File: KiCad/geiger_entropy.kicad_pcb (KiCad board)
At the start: 2 copper layers, 114.5 x 130.5 mm, 37 parts, among them J1 AudioJack2, J2 Conn_01x04_Socket, J3 Conn_01x10_Pin, J4 Conn_01x10_Pin, J5 Jack-DC, J6 ICSP, SW1 REV, SW2 FWD, SW3 RESET, U1 LM393, U2 ATmega328-P, U3 L7805, Y1 16MHz

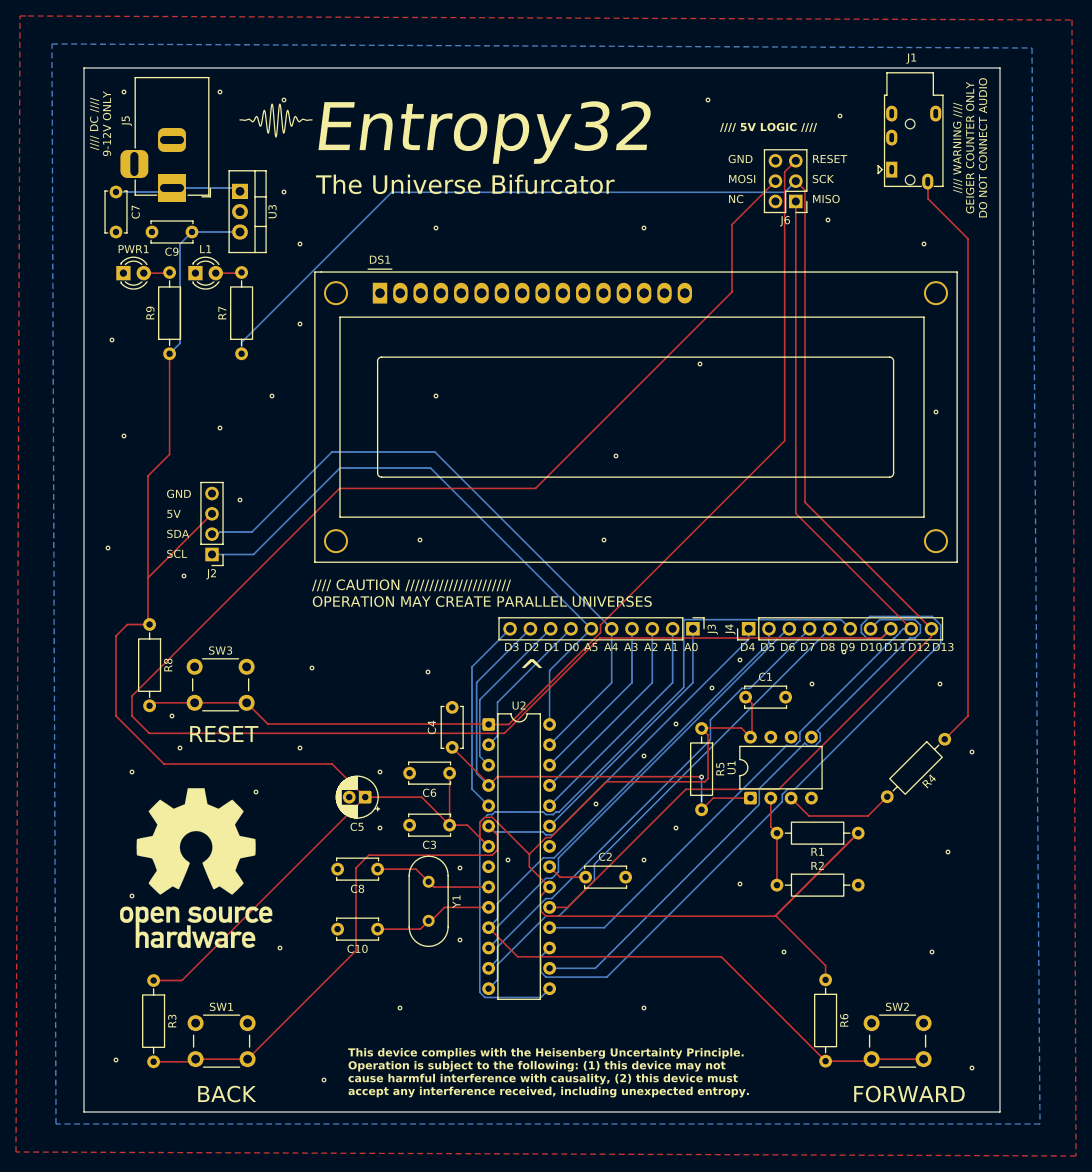
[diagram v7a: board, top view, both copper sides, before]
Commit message: Update PCB to add hysterisis to the LM393 comparator
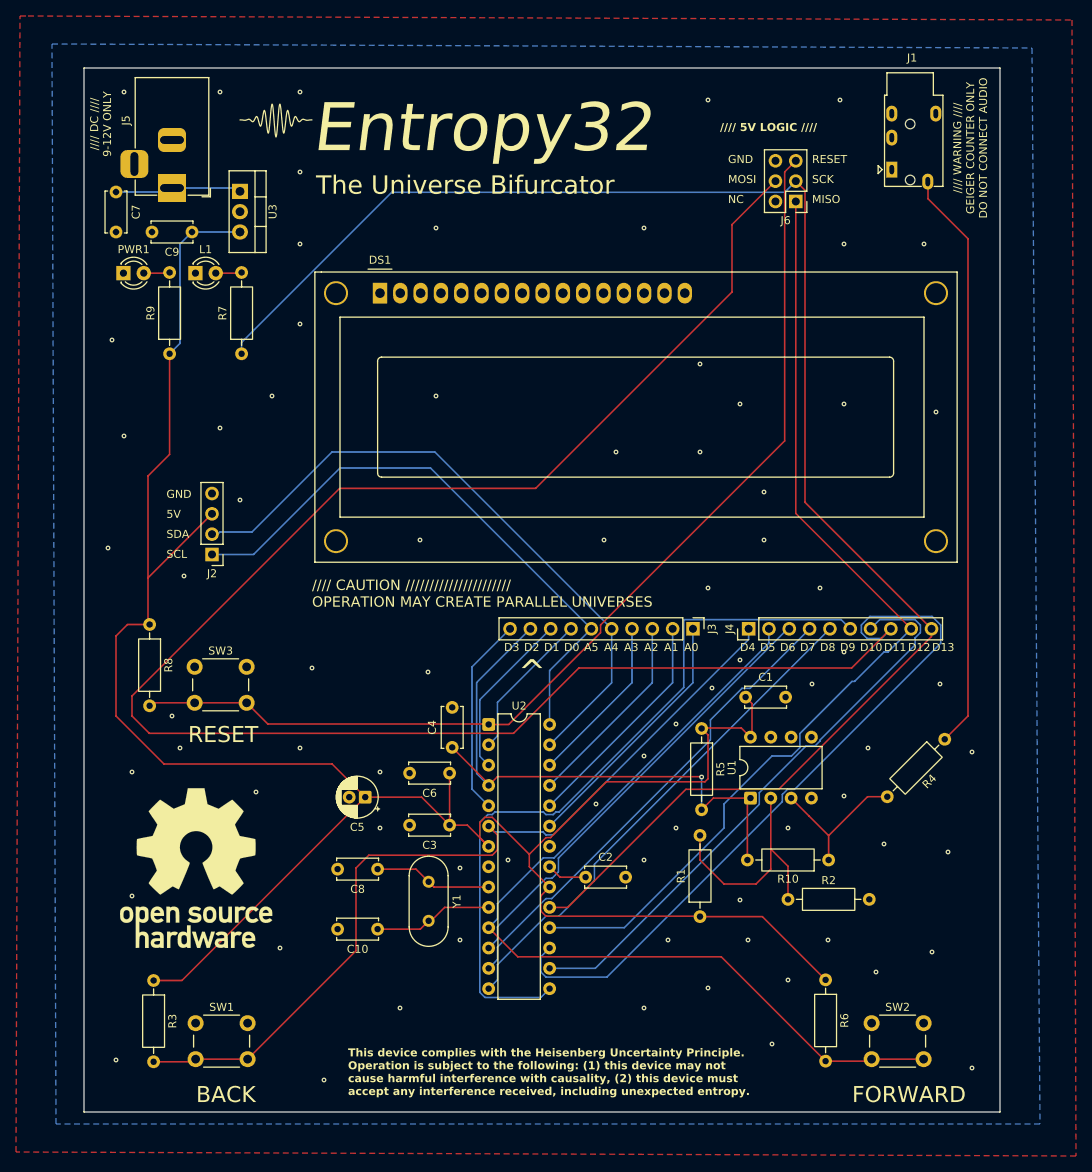
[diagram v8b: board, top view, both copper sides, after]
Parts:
- added R10: 100k, Resistor_THT:R_Axial_DIN0207_L6.3mm_D2.5mm_P10.16mm_Horizontal, F.Cu at (126.1, 127.0)
- moved R1 22.4 mm to (110.0, 134.1), turned to 90 degrees
- moved R2 2.25 mm to (121.0, 131.9)
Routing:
- net +5V: track 314.0 -> 283.8 mm
- net Net-(U1A--): track 11.2 -> 30.0 mm
- net /D2: track 67.5 -> 75.4 mm
- net /Geiger_pulse: track 13.9 -> 19.0 mm
- net /D12/MISO: track 120.9 -> 122.9 mm
- net /D10: track 74.4 -> 73.1 mm
- net GND: vias 59 -> 76
